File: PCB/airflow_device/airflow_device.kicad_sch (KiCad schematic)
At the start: 4 parts, among them J1 GRID_EYE Connector, J2 Grideye Servo, J3 Vent Servo, U1 esp32-wemos-d1-mini

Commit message: Adding more components
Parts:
- added C1: C, symbol Device:C
- added D1: LED, symbol Device:LED
- added J4: Conn_01x02_Pin, Connector_PinSocket_2.54mm:PinSocket_1x02_P2.54mm_Vertical, symbol Connector:Conn_01x02_Pin
- added L1: L, symbol Device:L
- added R1: R, symbol Device:R
- added U2: 3v3 regulator, Package_TO_SOT_THT:TO-220-3_Vertical, symbol Regulator_Linear:LD1117S33TR_SOT223

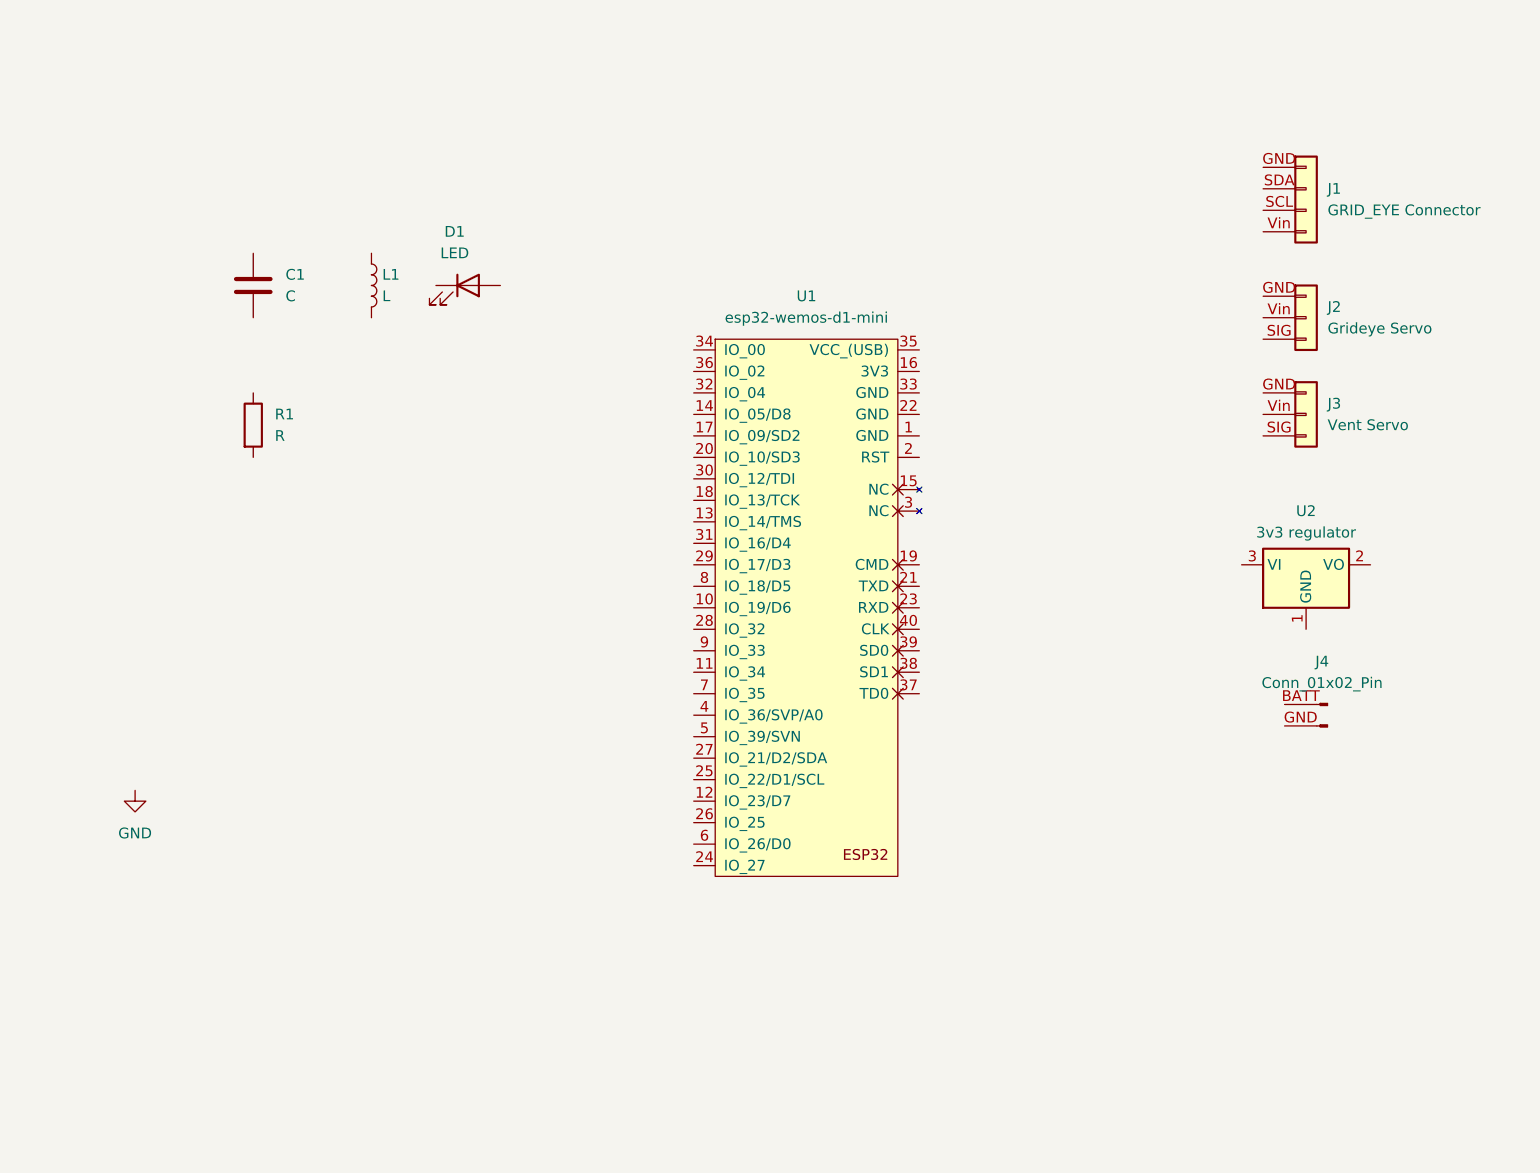
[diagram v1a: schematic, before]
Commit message: Adding more components, and fixing footprints
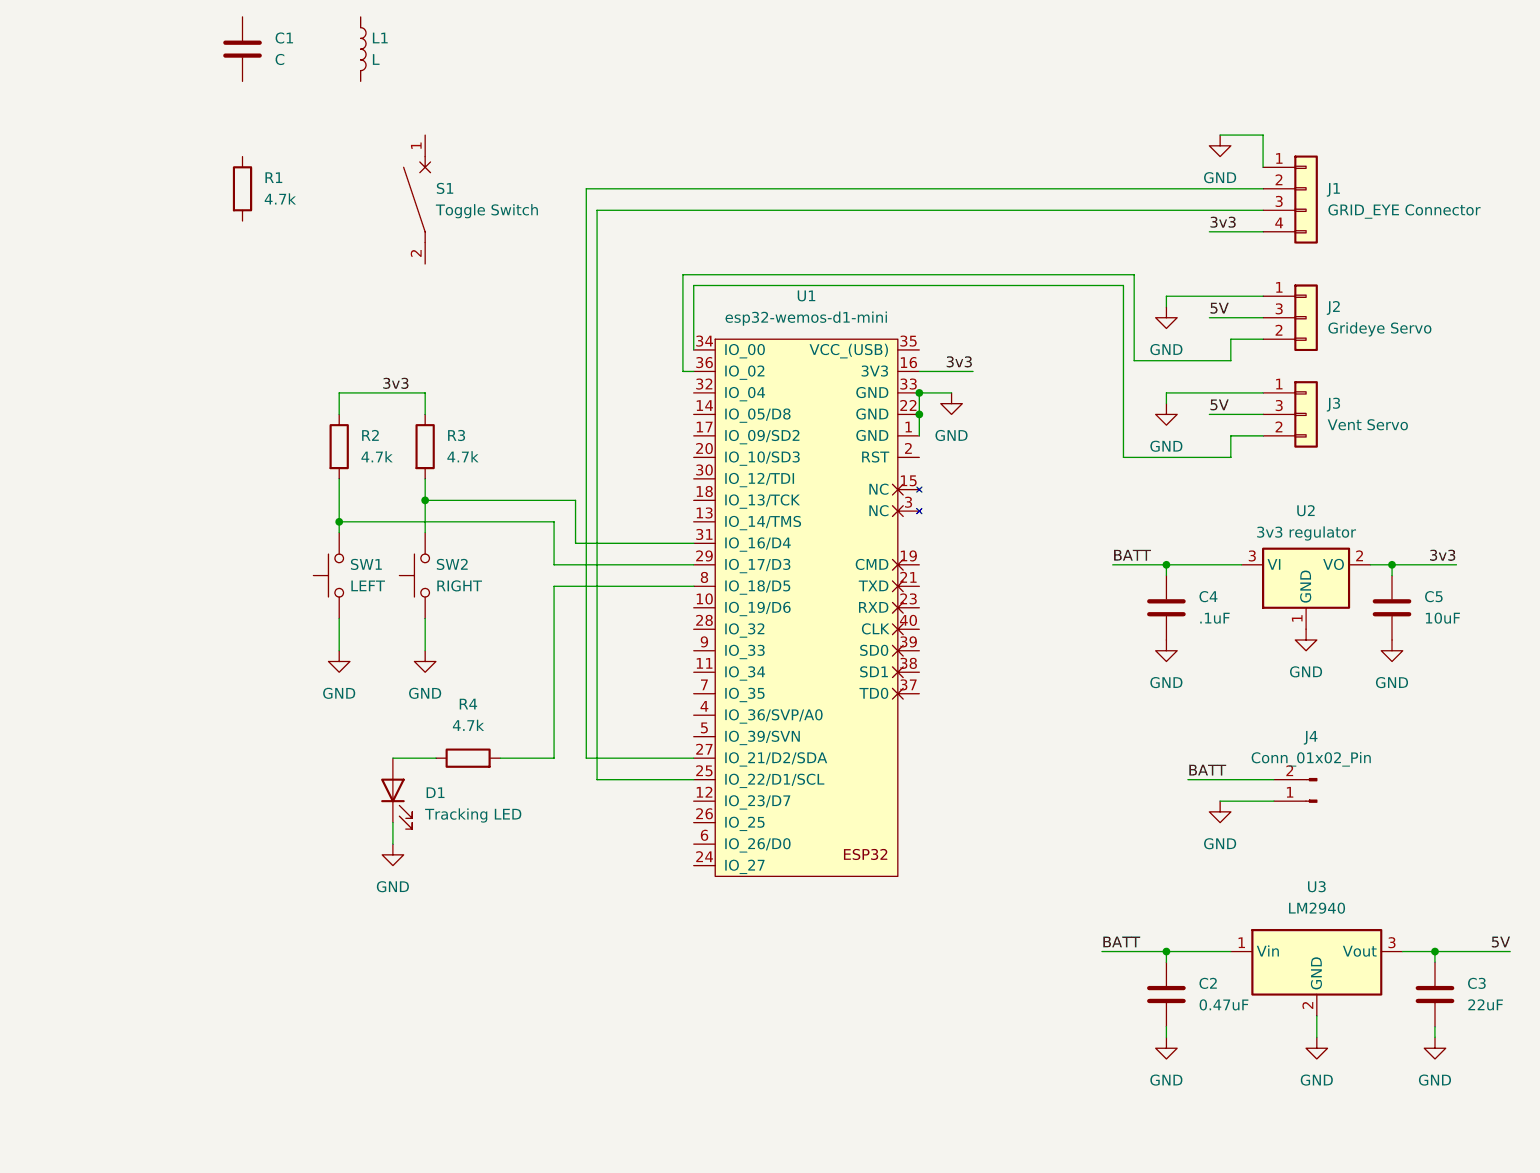
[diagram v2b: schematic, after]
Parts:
- added C2: 0.47uF, symbol Device:C
- added C3: 22uF, symbol Device:C
- added C4: .1uF, symbol Device:C
- added C5: 10uF, symbol Device:C
- added R2, R3, R4: 4.7k, symbol Device:R
- added S1: Toggle Switch, Connector_PinHeader_1.27mm:PinHeader_1x03_P1.27mm_Vertical, symbol Device:CircuitBreaker_1P
- added SW1: LEFT, symbol Switch:SW_Push
- added SW2: RIGHT, symbol Switch:SW_Push
- added U3: LM2940, Package_TO_SOT_THT:TO-220-3_Vertical, symbol Regulator_Switching:TSR1-2450E
- D1: value LED -> Tracking LED
- R1: value R -> 4.7k
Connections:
- net GND: now also D1.1 (K), J1.1 (GND), J2.1 (GND), J3.1 (GND), J4.1 (GND), U1.1 (GND), U1.22 (GND), U1.33 (GND), U2.1 (GND), C2.2, C3.2, C4.2, C5.2, SW1.1, SW2.1, U3.2 (GND)
- net at D1.2 (A): now also R4.1
- net 3v3: now reaches U2.2 (VO)
- net 3v3: now also J1.4 (Vin), U1.16 (3V3), C5.1, R2.1, R3.1
- net BATT: now reaches U2.3 (VI)
- net BATT: now also J4.2 (BATT), C2.1, C4.1, U3.1 (Vin)
- net at U1.25 (IO_22/D1/SCL): now also J1.3 (SCL)
- net at U1.27 (IO_21/D2/SDA): now also J1.2 (SDA)
- net at U1.29 (IO_17/D3): now also R2.2, SW1.2
- net at U1.31 (IO_16/D4): now also R3.2, SW2.2
- net at U1.34 (IO_00): now also J3.2 (SIG)
- net at U1.36 (IO_02): now also J2.2 (SIG)
- net at U1.8 (IO_18/D5): now also R4.2
- new net 5V: C3.1, J2.3 (Vin), J3.3 (Vin), U3.3 (Vout)
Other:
- moved on the sheet: C1, D1, J4, L1, R1

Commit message: Adding more footprints
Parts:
- C1, C2, C3, C4, C5: footprint (none) -> Capacitor_SMD:C_0805_2012Metric_Pad1.18x1.45mm_HandSolder
- D1: footprint (none) -> LED_THT:LED_D3.0mm
- R1, R2, R3, R4: footprint (none) -> Resistor_SMD:R_0805_2012Metric_Pad1.20x1.40mm_HandSolder
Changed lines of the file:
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@@
 			)
 		)
-		(property "Footprint" ""
+		(property "Footprint" "Resistor_SMD:R_0805_2012Metric_Pad1.20x1.40mm_HandSolder"
 			(at 79.502 54.61 90)
 			(effects
@@
 			)
 		)
-		(property "Footprint" ""
+		(property "Footprint" "LED_THT:LED_D3.0mm"
 			(at 99.06 125.73 0)
 			(effects
@@
 			)
 		)
-		(property "Footprint" ""
+		(property "Footprint" "Capacitor_SMD:C_0805_2012Metric_Pad1.18x1.45mm_HandSolder"
 			(at 218.1352 107.95 0)
 			(effects
@@
 			)
 		)
-		(property "Footprint" ""
+		(property "Footprint" "Resistor_SMD:R_0805_2012Metric_Pad1.20x1.40mm_HandSolder"
 			(at 101.092 85.09 90)
 			(effects
@@
 			)
 		)
-		(property "Footprint" ""
+		(property "Footprint" "Capacitor_SMD:C_0805_2012Metric_Pad1.18x1.45mm_HandSolder"
 			(at 223.2152 153.67 0)
 			(effects
@@
 			)
 		)
-		(property "Footprint" ""
+		(property "Footprint" "Capacitor_SMD:C_0805_2012Metric_Pad1.18x1.45mm_HandSolder"
 			(at 82.2452 41.91 0)
 			(effects
@@
 			)
 		)
-		(property "Footprint" ""
+		(property "Footprint" "Capacitor_SMD:C_0805_2012Metric_Pad1.18x1.45mm_HandSolder"
 			(at 191.4652 153.67 0)
 			(effects
@@
 			)
 		)
-		(property "Footprint" ""
+		(property "Footprint" "Resistor_SMD:R_0805_2012Metric_Pad1.20x1.40mm_HandSolder"
 			(at 90.932 85.09 90)
 			(effects
@@
 			)
 		)
-		(property "Footprint" ""
+		(property "Footprint" "Resistor_SMD:R_0805_2012Metric_Pad1.20x1.40mm_HandSolder"
 			(at 107.95 123.698 90)
 			(effects
@@
 			)
 		)
-		(property "Footprint" ""
+		(property "Footprint" "Capacitor_SMD:C_0805_2012Metric_Pad1.18x1.45mm_HandSolder"
 			(at 191.4652 107.95 0)
 			(effects

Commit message: Likely Functional PCB
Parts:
- removed C1: C, Capacitor_SMD:C_0805_2012Metric_Pad1.18x1.45mm_HandSolder, symbol Device:C
- removed L1: L, symbol Device:L
- removed S1: Toggle Switch, Connector_PinHeader_1.27mm:PinHeader_1x03_P1.27mm_Vertical, symbol Device:CircuitBreaker_1P
- removed SW2: RIGHT, symbol Switch:SW_Push
- added D2, D3: LED, LED_THT:LED_D3.0mm, symbol Device:LED
- added R5, R6, R7: 4.7k, Resistor_SMD:R_0805_2012Metric_Pad1.20x1.40mm_HandSolder, symbol Device:R
- added SW1: TOGGLE, Connector_PinHeader_2.54mm:PinHeader_1x03_P2.54mm_Vertical, symbol Switch:SW_SPDT
- added SW3: RIGHT, Button_Switch_THT:SW_PUSH_6mm_H5mm, symbol Switch:SW_Push
- added SW4: XTRA, Button_Switch_THT:SW_PUSH_6mm_H5mm, symbol Switch:SW_Push
- SW2: renamed from SW1; footprint (none) -> Button_Switch_THT:SW_PUSH_6mm_H5mm
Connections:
- net 3v3: now also R6.1, R7.1
- net GND: now also D2.1 (K), D3.1 (K), SW1.2 (B), SW3.1, SW4.1
- net at R1.1: now also D1.2 (A)
- net at R1.2: now also U1.12 (IO_23/D7)
- net at R4.1: now also D2.2 (A); no longer D1.2 (A)
- net at R3.2, U1.31 (IO_16/D4): now also SW3.2
- net SDA: now reaches J1.2 (SDA), U1.27 (IO_21/D2/SDA)
- net SCL: now reaches J1.3 (SCL), U1.25 (IO_22/D1/SCL)
- net at U1.10 (IO_19/D6): now also R5.2
- net at U1.14 (IO_05/D8): now also R4.2
- net at U1.6 (IO_26/D0): now also R7.2, SW4.2
- net at U1.8 (IO_18/D5): now also R6.2, SW1.3 (C); no longer R4.2
- new net: D3.2 (A), R5.1
- no-connect marks 0 -> 1
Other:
- moved on the sheet: D1, R2, R3, R4, SW2

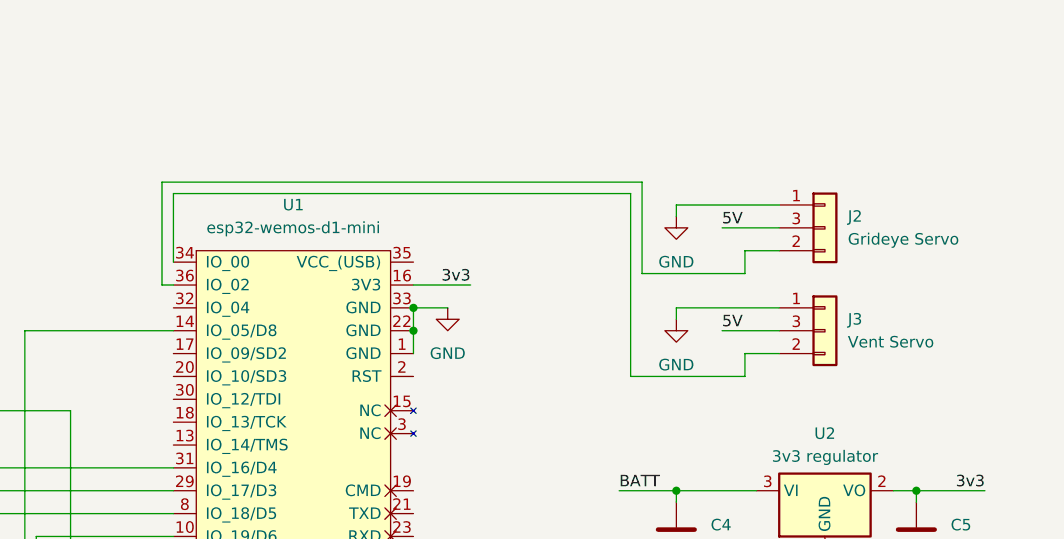
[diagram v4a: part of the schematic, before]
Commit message: Added 68uF caps for servos
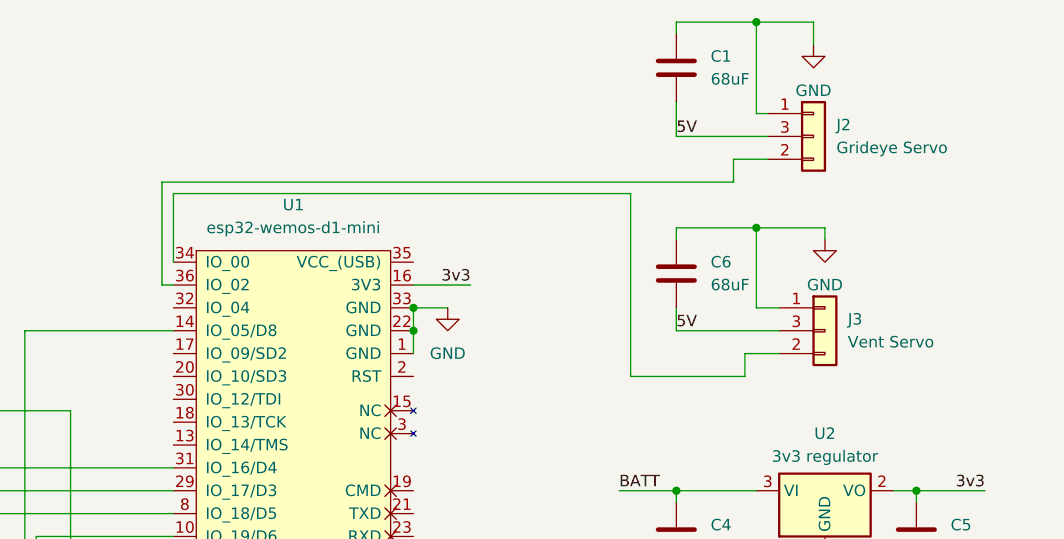
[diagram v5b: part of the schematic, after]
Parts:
- added C1, C6: 68uF, Capacitor_THT:CP_Radial_D7.5mm_P2.50mm, symbol Device:C
- J1: footprint Connector_Wire:SolderWire-0.5sqmm_1x04_P4.6mm_D0.9mm_OD2.1mm -> Connector_PinHeader_2.54mm:PinHeader_1x04_P2.54mm_Vertical
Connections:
- net 5V: now also C1.2, C6.2
- net GND: now also C1.1, C6.1
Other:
- moved on the sheet: J2

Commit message: PCB Done
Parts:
- removed R1: 4.7k, Resistor_SMD:R_0805_2012Metric_Pad1.20x1.40mm_HandSolder, symbol Device:R
- added TP1: 3.3V, TestPoint:TestPoint_Pad_2.5x2.5mm, symbol Connector:TestPoint
- added TP2: 5V, TestPoint:TestPoint_Pad_2.5x2.5mm, symbol Connector:TestPoint
- added TP3: GND, TestPoint:TestPoint_Pad_2.5x2.5mm, symbol Connector:TestPoint
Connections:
- net 3v3: now also TP1.1
- net 5V: now also TP2.1
- net GND: now also TP3.1
- net at J3.2 (SIG): now also U1.32 (IO_04); no longer U1.34 (IO_00)
- net at D1.2 (A): now also R6.2, SW1.3 (C), U1.8 (IO_18/D5)
